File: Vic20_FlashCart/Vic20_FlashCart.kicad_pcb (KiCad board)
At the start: 2 copper layers, 94.9 x 50 mm, 45 parts, among them U1 SST39LF040, U2 SST39LF040, U3 IS62C256AL, U4 7400, U5 74LS21

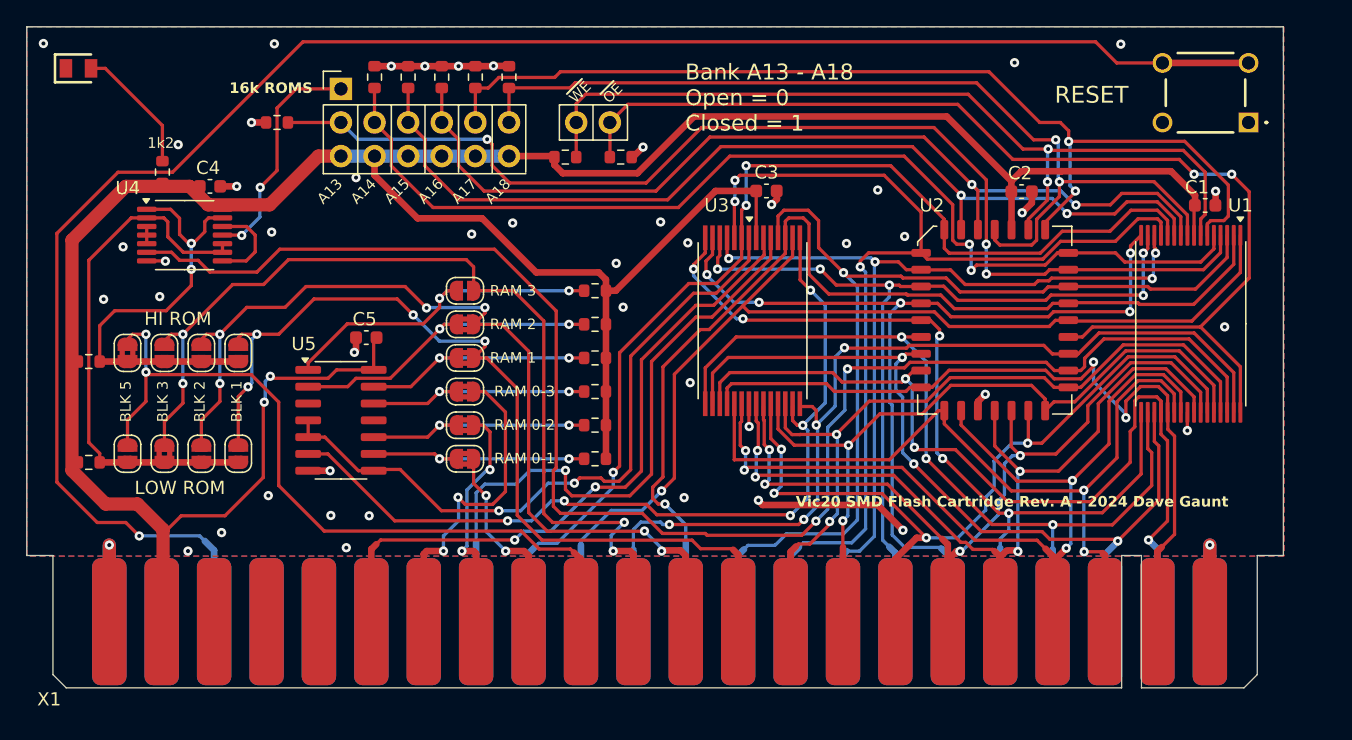
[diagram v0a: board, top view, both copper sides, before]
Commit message: - Updated Vic20 Flash Cart files to Ki-CAD 9.x - Cleaned up some component names and generated ibom's
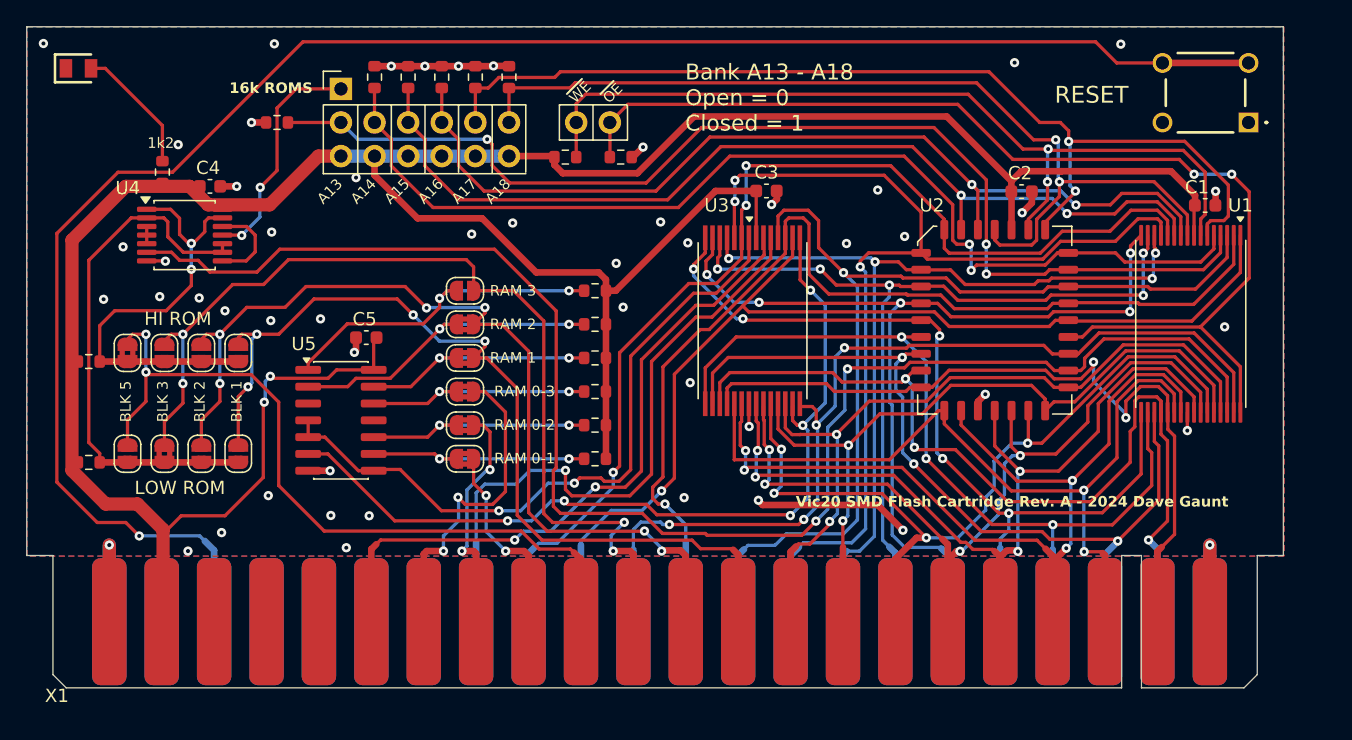
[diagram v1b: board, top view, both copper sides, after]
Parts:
- J3: value ~ -> Pin Headers
- U4: value 7400 -> SN74HCT00PWR
- U5: value 74LS21 -> CD74HCT21M96
- X1: value ~ -> Cart Fingers
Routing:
- net GND: vias 48 -> 52
